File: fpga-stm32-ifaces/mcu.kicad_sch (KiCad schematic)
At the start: 47 parts, among them J3 PMOD_HOST, J4 XILINX_JTAG, J5 CONN_01X03, U1 STM32H735-UFBGA176-25, U2 XC7S25-1FTGB196, U8 AT24MAC402, U9 ECS-1612MV-250-CN

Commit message: Finished initial schematic of fpga-stm32-ifaces board, waiting for sch review
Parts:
- added C55: 4.7 uF, azonenberg_pcb:EIA_0603_CAP_NOSILK, symbol device:C
- added C56: 0.47 uF, azonenberg_pcb:EIA_0402_CAP_NOSILK, symbol device:C
- added J10: CORTEX_DEBUG_ETM, symbol special-azonenberg:CORTEX_DEBUG_ETM
- added R73, R74, R76, R77: 33, azonenberg_pcb:EIA_0402_RES_NOSILK, symbol device:R
- added R75: 4.7K, azonenberg_pcb:EIA_0402_RES_NOSILK, symbol device:R
- added U16: W25Q128JV, azonenberg_pcb:DFN_8_1.27MM_6x5MM, symbol memory-azonenberg:W25Q80BV
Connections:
- net 3V3: now also C55.1, C56.1, J10.1 (VCC), R75.1, U16.8 (VCC)
- net FMC_AD9: now also U1.P6 (PA5); no longer U1.P12 (PE12)
- net GND: now also C55.2, C56.2, J10.11 (GND), J10.13 (GND), J10.15 (GND), J10.17 (GND), J10.19 (GND), J10.3 (GND), J10.5 (GND), J10.9 (GNDdet), U16.4 (GND)
- net MCU_FLASH_CS_N: now also R75.2, U16.1 (CS#)
- net MCU_FLASH_DQ0: now also R77.2
- net MCU_FLASH_DQ1: now also R73.1
- net MCU_FLASH_DQ2: now also R74.1
- net MCU_FLASH_DQ3: now also R76.2
- net MCU_FLASH_SCK: now also U16.6 (CLK)
- net MCU_JTAG_TCK: now also J10.4 (TCK)
- net MCU_JTAG_TDI: now also J10.8 (TDI)
- net MCU_JTAG_TDO: now also J10.6 (TDO)
- net MCU_JTAG_TMS: now also J10.2 (TMS)
- net MCU_RST_N: now also J10.10 (~{RST})
- net SUPER_SPI_CS_N: now also U1.B1 (PE4)
- net SUPER_SPI_MISO: now also U1.D3 (PE5)
- net SUPER_SPI_MOSI: now also U1.E3 (PE6)
- net SUPER_SPI_SCK: now also U1.P12 (PE12)
- net TRACECLK: now also J10.12 (TRACECLK)
- net TRACED0: now also J10.14 (TRACED0)
- net TRACED1: now also J10.16 (TRACED1)
- net TRACED2: now also J10.18 (TRACED2)
- net TRACED3: now also J10.20 (TRACED3)
- new net: R76.1, U16.7 (HOLD#/IO3)
- new net: R74.2, U16.3 (WP#/IO2)
- new net: R77.1, U16.5 (DI/IO0)
- new net: R73.2, U16.2 (DO/IO1)
- no-connect marks 2 -> 50
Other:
- note removed: "MCU external code flash"
- note removed: "TODO: ARM debug/trace connector"

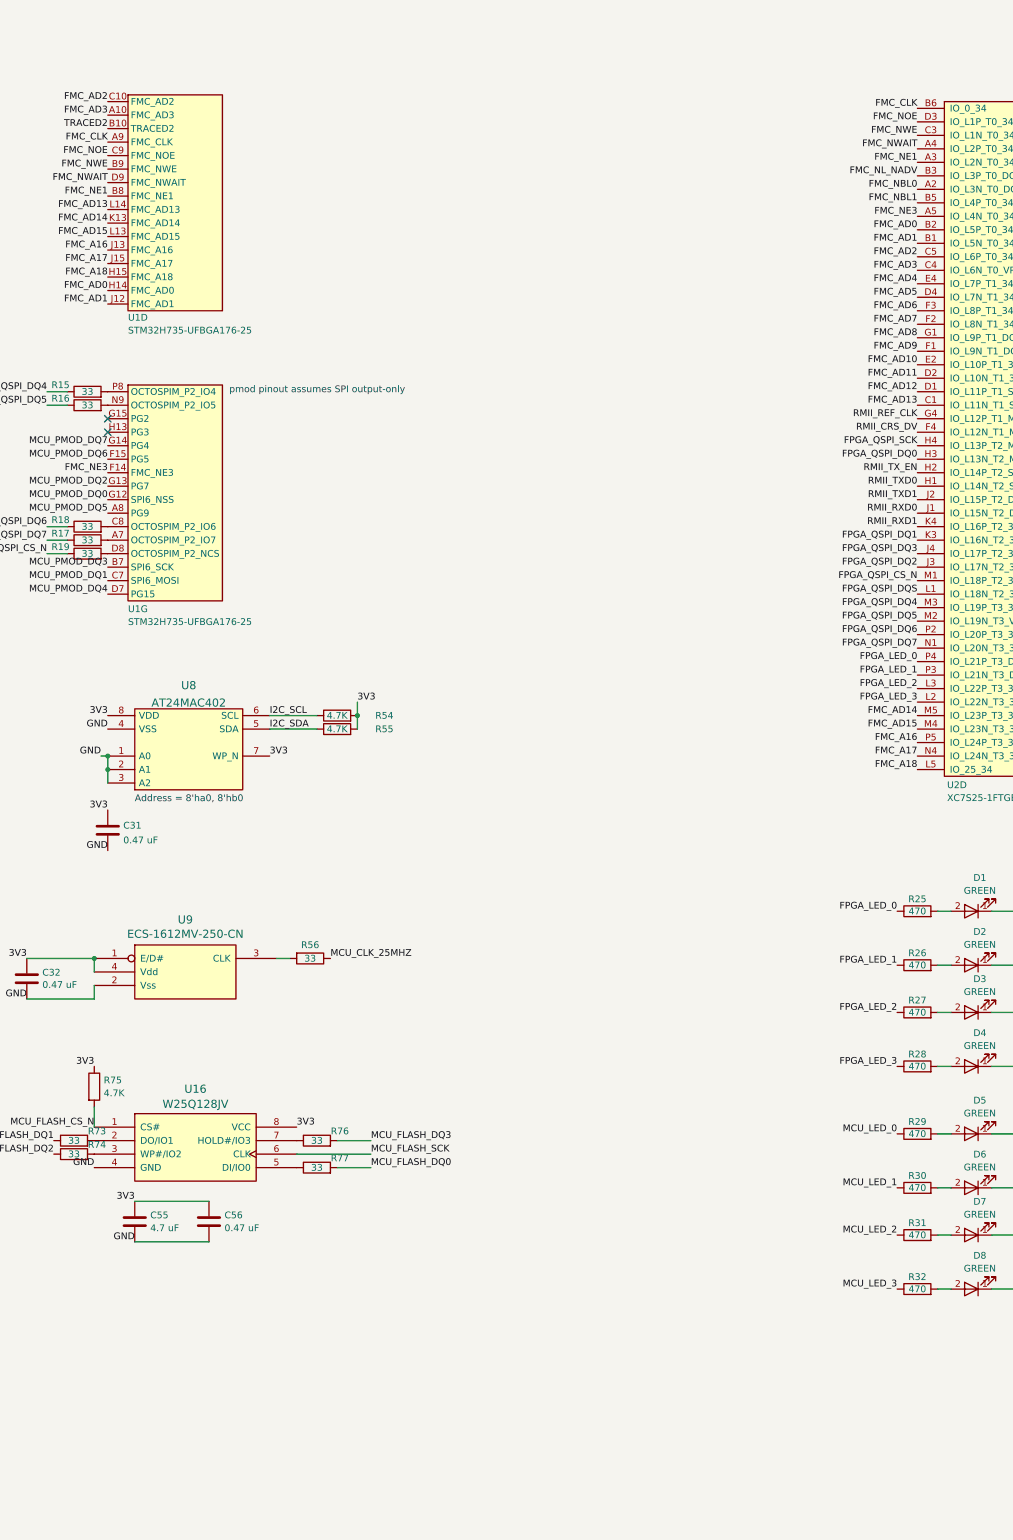
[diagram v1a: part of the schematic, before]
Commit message: Continued initial layout of fpga-stm32-ifaces
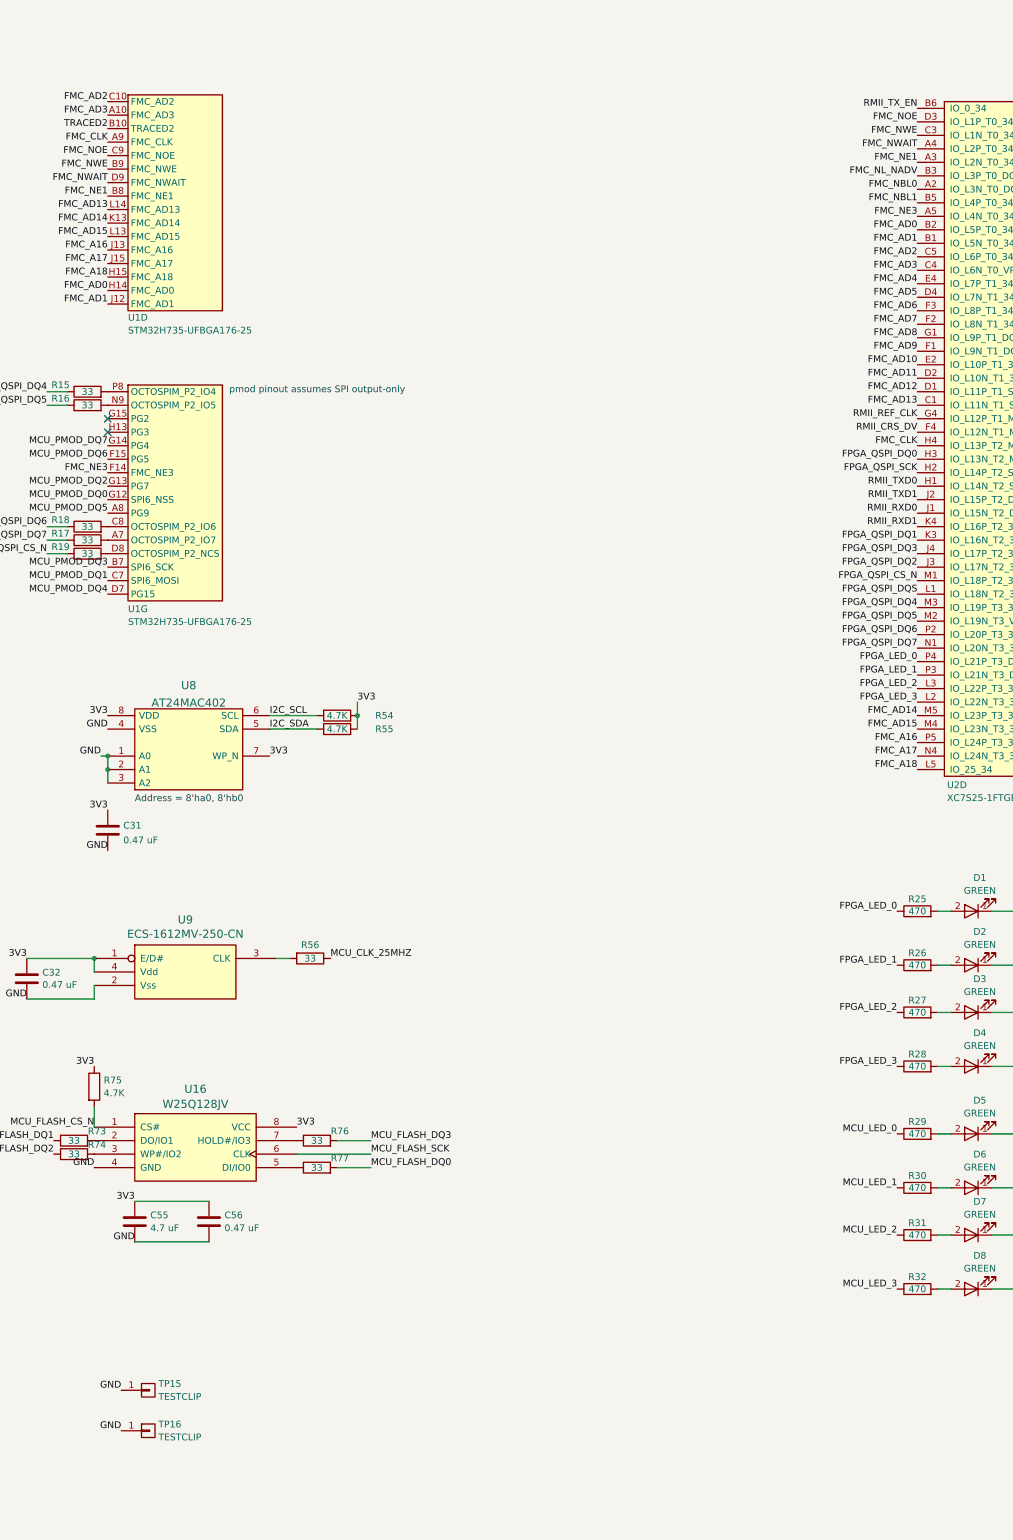
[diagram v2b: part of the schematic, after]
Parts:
- added TP15, TP16: TESTCLIP, azonenberg_pcb:TESTPOINT_SMT_KEYSTONE_5016, symbol conn:CONN_01X01
- D1, D2, D3, D4, D5, D6, D7, D8: footprint (none) -> azonenberg_pcb:EIA_0603_LED
- J10: footprint (none) -> azonenberg_pcb:CONN_HEADER_1.27MM_2x10_SMT_SAMTEC_FTSH-110-01-L-DV-K
- J3: footprint (none) -> azonenberg_pcb:CONN_HEADER_2.54MM_2x6_RA_PMOD_HOST
- R25, R26, R27, R28, R29, R30, R31, R32: footprint (none) -> azonenberg_pcb:EIA_0402_RES_NOSILK
- U1: footprint (none) -> azonenberg_pcb:BGA_201_10x10_DEPOP_0.65MM_OSHPARK
- U2: footprint (none) -> azonenberg_pcb:BGA_196_15x15_FULLARRAY_1MM_FTGB196
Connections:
- net FMC_CLK: now also U2.H4 (IO_L13P_T2_MRCC_34); no longer U2.B6 (IO_0_34)
- net FPGA_QSPI_SCK: now also U2.H2 (IO_L14P_T2_SRCC_34); no longer U2.H4 (IO_L13P_T2_MRCC_34)
- net GND: now also TP15.1 (P1), TP16.1 (P1)
- net RMII_TX_EN: now also U2.B6 (IO_0_34); no longer U2.H2 (IO_L14P_T2_SRCC_34)
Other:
- company: (none) -> Antikernel Labs
- title: (none) -> FPGA - STM32 Interface Test
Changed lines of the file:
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@@
 	(generator_version "8.0")
 	(paper "A2")
+	(title_block
+		(title "FPGA - STM32 Interface Test")
+		(date "2024-06-12")
+		(rev "0.1")
+		(company "Antikernel Labs")
+	)
 	(junction
 		(at 39.37 365.76)
@@
 		)
 	)
+	(label "GND"
+		(at 189.23 278.13 180)
+		(fields_autoplaced yes)
+		(effects
+			(font
+				(size 1.27 1.27)
+			)
+			(justify right bottom)
+		)
+	)
 	(label "TRACECLK"
 		(at 40.64 95.25 180)
@@
 	)
 	(label "RMII_TX_EN"
-		(at 339.09 105.41 180)
+		(at 339.09 36.83 180)
 		(fields_autoplaced yes)
 		(effects
@@
 	)
 	(label "FPGA_QSPI_SCK"
-		(at 339.09 100.33 180)
+		(at 339.09 105.41 180)
 		(fields_autoplaced yes)
 		(effects
@@
 	)
 	(label "FMC_CLK"
-		(at 339.09 36.83 180)
+		(at 339.09 100.33 180)
 		(fields_autoplaced yes)
 		(effects
@@
 		)
 	)
+	(label "GND"
+		(at 189.23 285.75 180)
+		(fields_autoplaced yes)
+		(effects
+			(font
+				(size 1.27 1.27)
+			)
+			(justify right bottom)
+		)
+	)
 	(label "RMII_REF_CLK"
 		(at 40.64 35.56 180)
@@
 			)
 		)
-		(property "Footprint" ""
+		(property "Footprint" "azonenberg_pcb:EIA_0603_LED"
 			(at 349.25 207.01 0)
 			(effects
@@
 			)
 		)
-		(property "Footprint" ""
+		(property "Footprint" "azonenberg_pcb:EIA_0402_RES_NOSILK"
 			(at 339.09 260.858 90)
 			(effects
@@
 			)
 		)
-		(property "Footprint" ""
+		(property "Footprint" "azonenberg_pcb:EIA_0603_LED"
 			(at 349.25 187.96 0)
 			(effects
@@
 			)
 		)
-		(property "Footprint" ""
+		(property "Footprint" "azonenberg_pcb:EIA_0603_LED"
 			(at 349.25 198.12 0)
 			(effects
@@
 			)
 		)
-		(property "Footprint" ""
+		(property "Footprint" "azonenberg_pcb:EIA_0402_RES_NOSILK"
 			(at 339.09 189.738 90)
 			(effects
@@
 			)
 		)
-		(property "Footprint" ""
+		(property "Footprint" "azonenberg_pcb:BGA_201_10x10_DEPOP_0.65MM_OSHPARK"
 			(at 138.43 74.93 0)
 			(effects
@@
 			)
 		)
-		(property "Footprint" ""
+		(property "Footprint" "azonenberg_pcb:EIA_0402_RES_NOSILK"
 			(at 339.09 199.898 90)
 			(effects
@@
 			)
 		)
-		(property "Footprint" ""
+		(property "Footprint" "azonenberg_pcb:BGA_201_10x10_DEPOP_0.65MM_OSHPARK"
 			(at 138.43 129.54 0)
 			(effects
@@
 			)
 		)
-		(property "Footprint" ""
+		(property "Footprint" "azonenberg_pcb:BGA_201_10x10_DEPOP_0.65MM_OSHPARK"
 			(at 190.5 129.54 0)
 			(effects
@@
 			)
 		)
-		(property "Footprint" ""
+		(property "Footprint" "azonenberg_pcb:EIA_0402_RES_NOSILK"
 			(at 339.09 231.648 90)
 			(effects
@@
 			)
 		)
-		(property "Footprint" ""
+		(property "Footprint" "azonenberg_pcb:CONN_HEADER_1.27MM_2x10_SMT_SAMTEC_FTSH-110-01-L-DV-K"
 			(at 46.99 337.566 0)
 			(effects
@@
 			)
 		)
-		(property "Footprint" ""
+		(property "Footprint" "azonenberg_pcb:BGA_201_10x10_DEPOP_0.65MM_OSHPARK"
 			(at 44.45 129.54 0)
 			(effects
@@
 	)
 	(symbol
+		(lib_id "conn:CONN_01X01")
+		(at 194.31 285.75 0)
+		(unit 1)
+		(exclude_from_sim no)
+		(in_bom yes)
+		(on_board yes)
+		(dnp no)
+		(fields_autoplaced yes)
+		(property "Reference" "TP16"
+			(at 196.215 284.5378 0)
+			(effects
+				(font
+					(size 1.27 1.27)
+				)
+				(justify left)
+			)
+		)
+		(property "Value" "TESTCLIP"
+			(at 196.215 286.9621 0)
+			(effects
+				(font
+					(size 1.27 1.27)
+				)
+				(justify left)
+			)
+		)
+		(property "Footprint" "azonenberg_pcb:TESTPOINT_SMT_KEYSTONE_5016"
+			(at 194.31 285.75 0)
+			(effects
+				(font
+					(size 1.27 1.27)
+				)
+				(hide yes)
+			)
+		)
+		(property "Datasheet" ""
+			(at 194.31 285.75 0)
+			(effects
+				(font
+					(size 1.27 1.27)
+				)
+				(hide yes)
+			)
+		)
+		(property "Description" "Connector, single row, 01x01, pin header"
+			(at 194.31 285.75 0)
+			(effects
+				(font
+					(size 1.27 1.27)
+				)
+				(hide yes)
+			)
+		)
+		(pin "1"
+		)
+		(instances
+			(project "fpga-stm32-ifaces"
+				(path "/b35a72f3-8995-417e-af27-dca34b6125a3/89442227-c436-4e13-9216-152fa3ab5112"
+					(reference "TP16")
+					(unit 1)
+				)
+			)
+		)
+	)
+	(symbol
 		(lib_id "device:R")
 		(at 226.06 236.22 90)
@@
 	)
 	(symbol
+		(lib_id "conn:CONN_01X01")
+		(at 194.31 278.13 0)
+		(unit 1)
+		(exclude_from_sim no)
+		(in_bom yes)
+		(on_board yes)
+		(dnp no)
+		(fields_autoplaced yes)
+		(property "Reference" "TP15"
+			(at 196.215 276.9178 0)
+			(effects
+				(font
+					(size 1.27 1.27)
+				)
+				(justify left)
+			)
+		)
+		(property "Value" "TESTCLIP"
+			(at 196.215 279.3421 0)
+			(effects
+				(font
+					(size 1.27 1.27)
+				)
+				(justify left)
+			)
+		)
+		(property "Footprint" "azonenberg_pcb:TESTPOINT_SMT_KEYSTONE_5016"
+			(at 194.31 278.13 0)
+			(effects
+				(font
+					(size 1.27 1.27)
+				)
+				(hide yes)
+			)
+		)
+		(property "Datasheet" ""
+			(at 194.31 278.13 0)
+			(effects
+				(font
+					(size 1.27 1.27)
+				)
+				(hide yes)
+			)
+		)
+		(property "Description" "Connector, single row, 01x01, pin header"
+			(at 194.31 278.13 0)
+			(effects
+				(font
+					(size 1.27 1.27)
+				)
+				(hide yes)
+			)
+		)
+		(pin "1"
+		)
+		(instances
+			(project "fpga-stm32-ifaces"
+				(path "/b35a72f3-8995-417e-af27-dca34b6125a3/89442227-c436-4e13-9216-152fa3ab5112"
+					(reference "TP15")
+					(unit 1)
+				)
+			)
+		)
+	)
+	(symbol
 		(lib_id "device:R")
 		(at 184.15 220.98 0)
@@
 			)
 		)
-		(property "Footprint" ""
+		(property "Footprint" "azonenberg_pcb:EIA_0603_LED"
 			(at 349.25 217.17 0)
 			(effects
@@
 			)
 		)
-		(property "Footprint" ""
+		(property "Footprint" "azonenberg_pcb:BGA_201_10x10_DEPOP_0.65MM_OSHPARK"
 			(at 95.25 129.54 0)
 			(effects
@@
 			)
 		)
-		(property "Footprint" ""
+		(property "Footprint" "azonenberg_pcb:EIA_0402_RES_NOSILK"
 			(at 339.09 218.948 90)
 			(effects
@@
 			)
 		)
-		(property "Footprint" ""
+		(property "Footprint" "azonenberg_pcb:EIA_0603_LED"
 			(at 349.25 259.08 0)
 			(effects
@@
 			)
 		)
-		(property "Footprint" ""
+		(property "Footprint" "azonenberg_pcb:EIA_0603_LED"
 			(at 349.25 248.92 0)
 			(effects
@@
 			)
 		)
-		(property "Footprint" ""
+		(property "Footprint" "azonenberg_pcb:BGA_201_10x10_DEPOP_0.65MM_OSHPARK"
 			(at 190.5 74.93 0)
 			(effects
@@
 			)
 		)
-		(property "Footprint" ""
+		(property "Footprint" "azonenberg_pcb:EIA_0603_LED"
 			(at 349.25 240.03 0)
 			(effects
@@
 			)
 		)
-		(property "Footprint" ""
+		(property "Footprint" "azonenberg_pcb:EIA_0402_RES_NOSILK"
 			(at 339.09 250.698 90)
 			(effects
@@
 			)
 		)
-		(property "Footprint" ""
+		(property "Footprint" "azonenberg_pcb:EIA_0603_LED"
 			(at 349.25 229.87 0)
 			(effects
@@
 			)
 		)
-		(property "Footprint" ""
+		(property "Footprint" "azonenberg_pcb:CONN_HEADER_2.54MM_2x6_RA_PMOD_HOST"
 			(at 412.75 195.58 0)
 			(effects
@@
 			)
 		)
-		(property "Footprint" ""
+		(property "Footprint" "azonenberg_pcb:BGA_196_15x15_FULLARRAY_1MM_FTGB196"
 			(at 344.17 162.56 0)
 			(effects
@@
 			)
 		)
-		(property "Footprint" ""
+		(property "Footprint" "azonenberg_pcb:EIA_0402_RES_NOSILK"
 			(at 339.09 208.788 90)
 			(effects
@@
 			)
 		)
-		(property "Footprint" ""
+		(property "Footprint" "azonenberg_pcb:BGA_201_10x10_DEPOP_0.65MM_OSHPARK"
 			(at 95.25 74.93 0)
 			(effects
@@
 			)
 		)
-		(property "Footprint" ""
+		(property "Footprint" "azonenberg_pcb:EIA_0402_RES_NOSILK"
 			(at 339.09 241.808 90)
 			(effects
@@
 			)
 		)
-		(property "Footprint" ""
+		(property "Footprint" "azonenberg_pcb:BGA_201_10x10_DEPOP_0.65MM_OSHPARK"
 			(at 44.45 74.93 0)
 			(effects

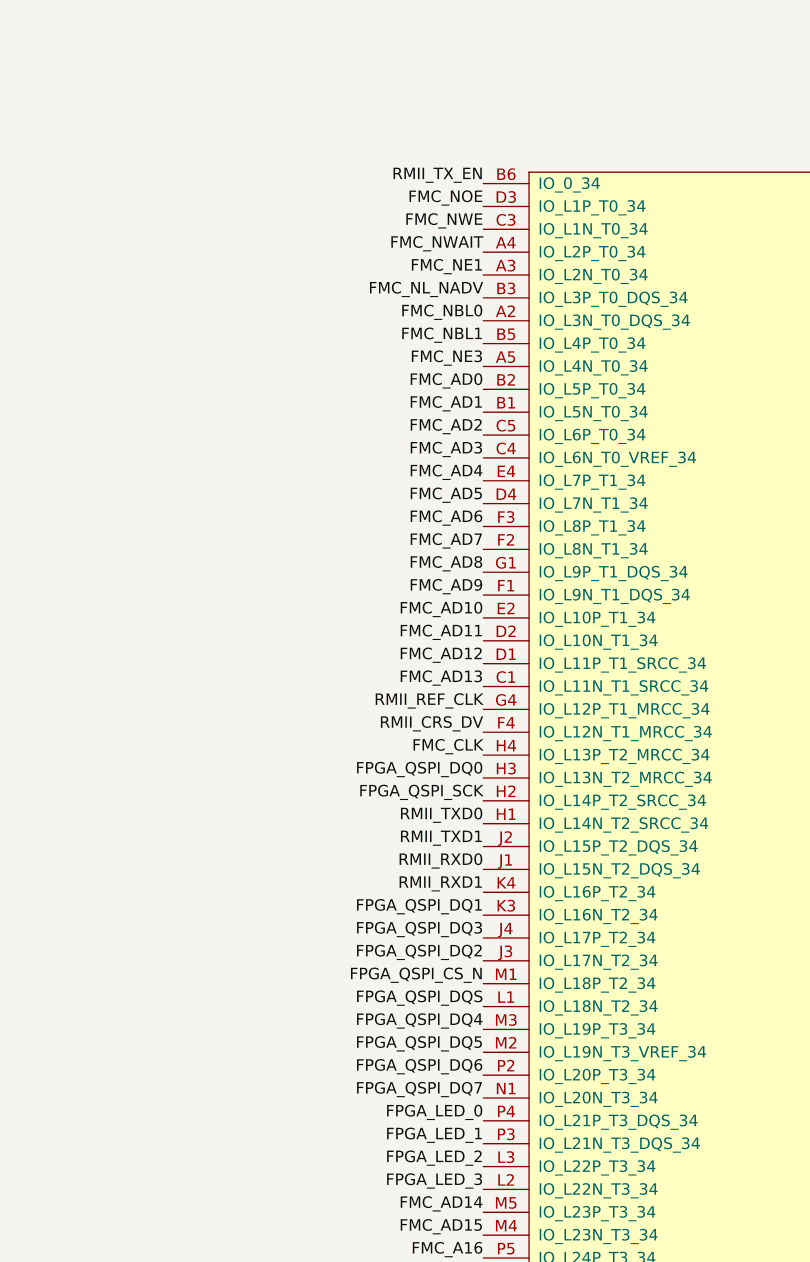
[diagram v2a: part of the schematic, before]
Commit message: Initial routing of FPGA power
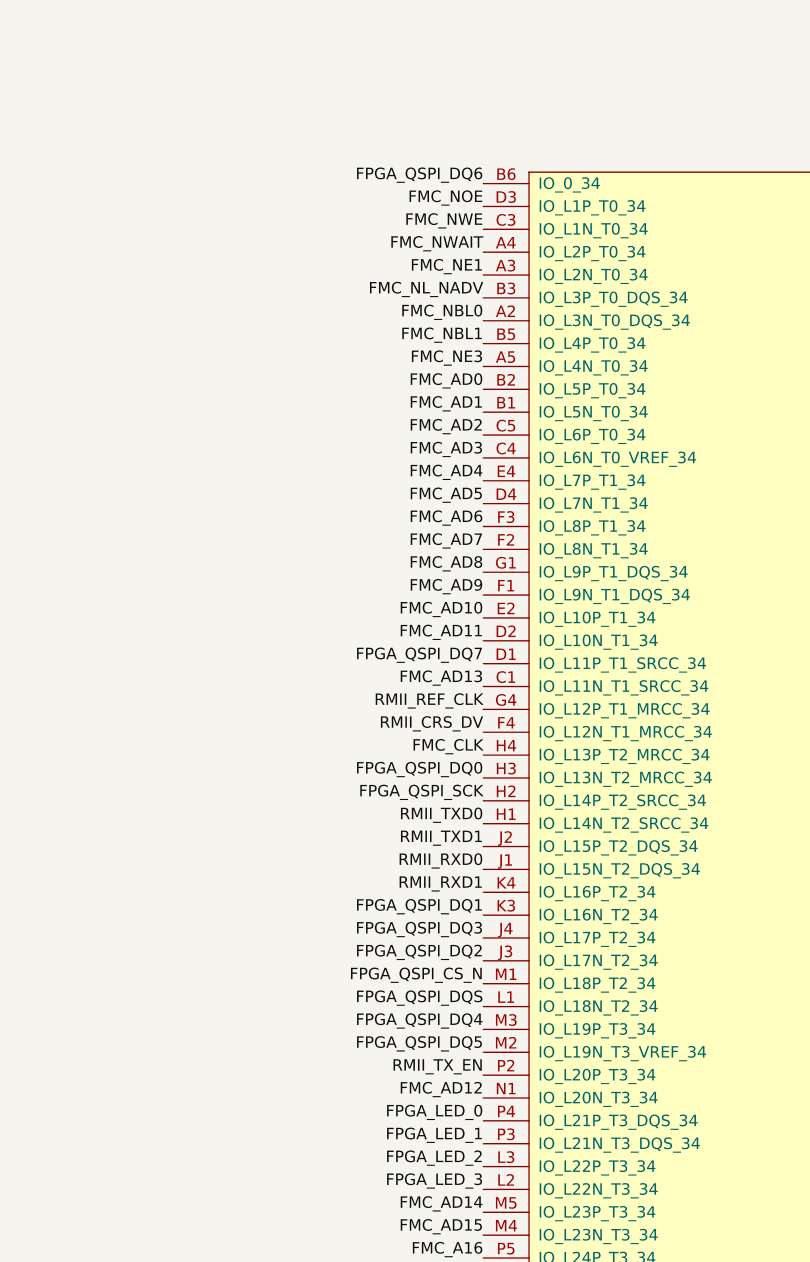
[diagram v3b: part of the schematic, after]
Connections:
- net FMC_AD12: now also U2.N1 (IO_L20N_T3_34); no longer U2.D1 (IO_L11P_T1_SRCC_34)
- net FPGA_QSPI_DQ6: now also U2.B6 (IO_0_34); no longer U2.P2 (IO_L20P_T3_34)
- net FPGA_QSPI_DQ7: now also U2.D1 (IO_L11P_T1_SRCC_34); no longer U2.N1 (IO_L20N_T3_34)
- net RMII_TX_EN: now also U2.P2 (IO_L20P_T3_34); no longer U2.B6 (IO_0_34)
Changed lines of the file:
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@@
 	)
 	(label "FPGA_QSPI_DQ7"
-		(at 339.09 138.43 180)
+		(at 339.09 90.17 180)
 		(fields_autoplaced yes)
 		(effects
@@
 	)
 	(label "RMII_TX_EN"
-		(at 339.09 36.83 180)
+		(at 339.09 135.89 180)
 		(fields_autoplaced yes)
 		(effects
@@
 	)
 	(label "FMC_AD12"
-		(at 339.09 90.17 180)
+		(at 339.09 138.43 180)
 		(fields_autoplaced yes)
 		(effects
@@
 	)
 	(label "FPGA_QSPI_DQ6"
-		(at 339.09 135.89 180)
-		(fields_autoplaced yes)
-		(effects
+		(at 339.09 36.83 180)
+		(fields_autoplaced yes)
+		(effects
